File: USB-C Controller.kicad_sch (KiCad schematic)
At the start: 23 parts, among them J4 BM04B-SRSS-TB, Q5 AO4459, U3 STUSB4500QTR

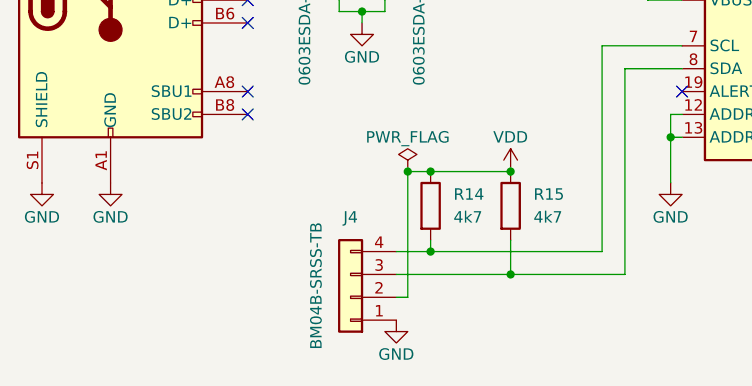
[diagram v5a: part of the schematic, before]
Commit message: Replace JST SH connector symbol with Mounting Pin version
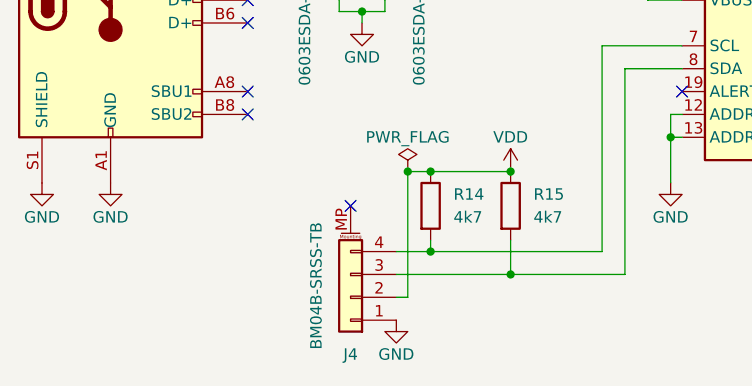
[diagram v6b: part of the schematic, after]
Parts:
- J4: symbol Connector_Generic:Conn_01x04 -> Connector_Generic_MountingPin:Conn_01x04_MountingPin
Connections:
- no-connect marks 11 -> 12
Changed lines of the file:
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@@
   )
   (no_connect (at 189.23 99.06))
+  (no_connect (at 104.14 135.89))
   (no_connect (at 92.71 115.57))
   (no_connect (at 92.71 110.49))
@@
     (pin "2")
   )
-  (symbol (lib_id "Connector_Generic:Conn_01x04") (at 104.14 146.05 180) (unit 1)
-    (in_bom yes) (on_board yes)
-    (property "Reference" "J4" (id 0) (at 104.14 137.16 0))
+  (symbol (lib_id "Connector_Generic_MountingPin:Conn_01x04_MountingPin") (at 104.14 146.05 180) (unit 1)
+    (in_bom yes) (on_board yes)
+    (property "Reference" "J4" (id 0) (at 104.14 152.4 0))
     (property "Value" "BM04B-SRSS-TB" (id 1) (at 100.33 144.78 90))
     (property "Footprint" "Connector_JST:JST_SH_BM04B-SRSS-TB_1x04-1MP_P1.00mm_Vertical" (id 2) (at 104.14 146.05 0)
@@
     (pin "3")
     (pin "4")
+    (pin "MP")
   )
   (symbol (lib_id "power:VDD") (at 121.92 132.08 0) (unit 1)

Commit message: Initial board layout
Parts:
- J3: value (none) -> TYPE-C-31-M-12; footprint (none) -> Connector_USB:USB_C_Receptacle_HRO_TYPE-C-31-M-12
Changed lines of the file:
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@@
     (in_bom yes) (on_board yes)
     (property "Reference" "J3" (id 0) (at 77.47 87.63 0))
-    (property "Value" "" (id 1) (at 77.47 90.17 0))
-    (property "Footprint" "" (id 2) (at 81.28 110.49 0)
+    (property "Value" "TYPE-C-31-M-12" (id 1) (at 77.47 90.17 0))
+    (property "Footprint" "Connector_USB:USB_C_Receptacle_HRO_TYPE-C-31-M-12" (id 2) (at 81.28 110.49 0)
       (effects (font (size 1.27 1.27)) hide)
     )
